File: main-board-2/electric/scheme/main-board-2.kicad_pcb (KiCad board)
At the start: 2 copper layers, 85 x 56 mm, 124 parts, among them K1 power-switch, K2 usb-power-switch, P1 batt, P10 rst, P11 screw-1, P13 screw-2, P14 gpio-big, P15 gpio-small, P16 moto-1, P17 moto-2, P3 trigger-btn, P4 CONN_3X2, P5 reg-short-to-gnd-1, P6 reg-short-to-gnd-2, P7 bootloader, P8 cross board conn, P9 rst, Q1 IRLML2244, Q10 IRLML2244, Q11 sot223, Q12 bc857, Q13 irlml2244, Q2 BC847, Q3 IRLML2244, Q4 IRLML2244, Q5 BC847, Q6 BC847, Q7 BC847, Q8 BC847, Q9 IRLML2244, U1 LM317AEMP, U2 LM317AT, U3 LM317AEMP, U4 LM317AT, U5 LM293, U6 L298, U7 MINI-USB-B, X1 8MHz

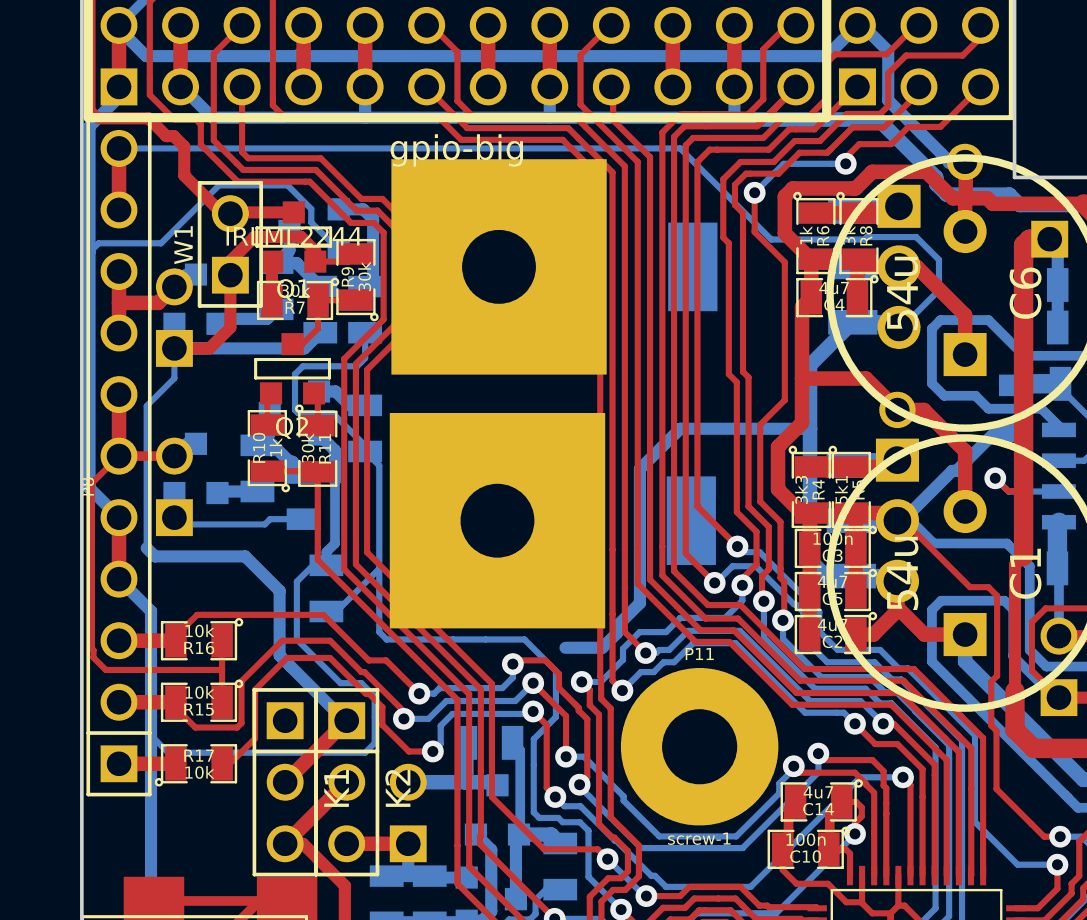
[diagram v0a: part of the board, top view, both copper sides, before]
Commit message: Changed packages to vertical ones.
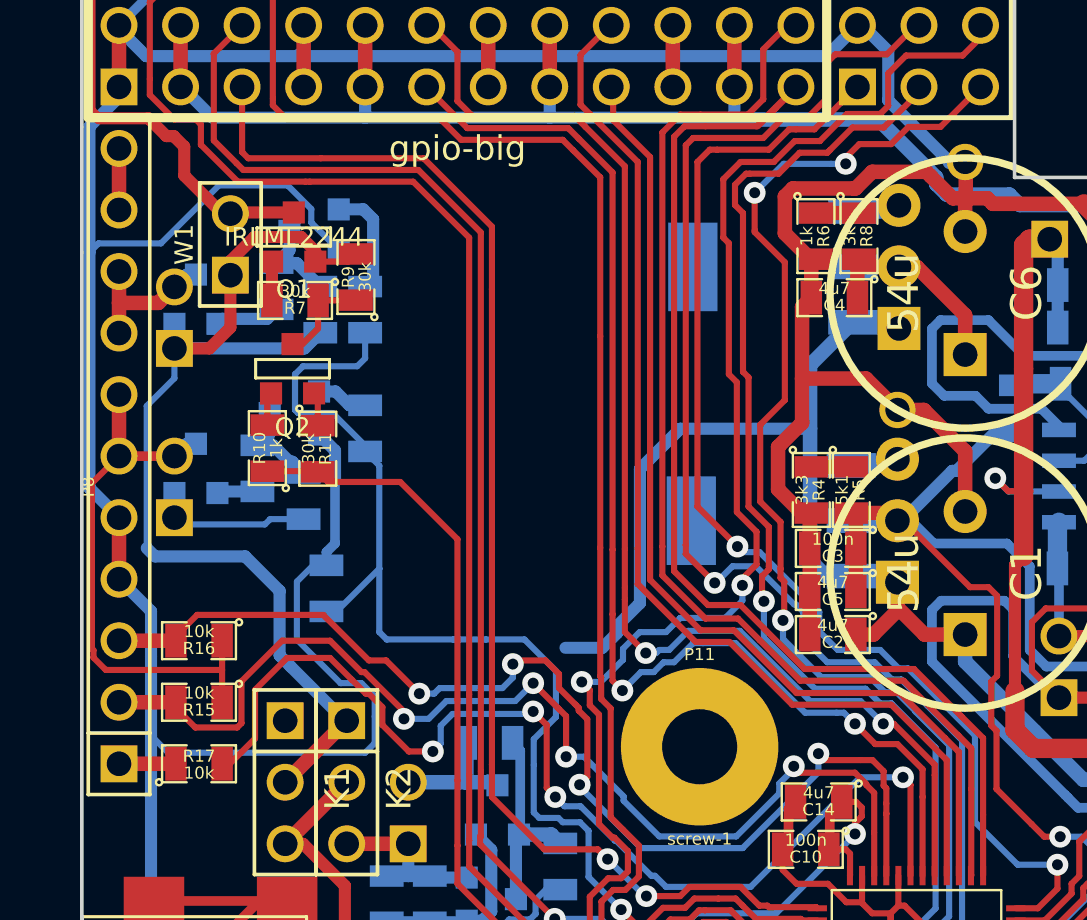
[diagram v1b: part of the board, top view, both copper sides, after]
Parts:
- U2, U4: footprint my_TO220 -> my_TO220_VERT
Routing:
- net /batt+: track 207.3 -> 164.3 mm
- net N-0000085: track 5.54 -> 3.47 mm
- net /rpi-pwr-en: track 49.0 -> 50.7 mm
- net N-0000086: track 6.06 -> 4.42 mm
- net /gpio-5: track 59.1 -> 59.8 mm
- net /gpio-1: track 52.9 -> 53.5 mm
- net /sda-rpi: track 77.5 -> 78.1 mm

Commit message: Routing...
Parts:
- moved R24 6.24 mm to (158.9, 153.3), turned to 0 degrees
- moved R22 6.10 mm to (161.2, 143.7)
- moved Q5 5.66 mm to (158.3, 143.8)
- moved Q6 5.08 mm to (157.1, 150.7)
- moved R11 4.98 mm to (157.9, 152.5)
- moved Q2 4.91 mm to (156.8, 149.2)
- moved R10 4.90 mm to (155.7, 152.5)
- moved R18 4.89 mm to (156.1, 142.2), turned to 180 degrees
- moved R19 4.89 mm to (154.9, 149.0), turned to 180 degrees
- moved Q3 4.66 mm to (152.8, 143.7), turned to 90 degrees
- moved R23 4.59 mm to (159.7, 150.7)
- moved R7 4.06 mm to (155.9, 146.5)
- moved R9 3.96 mm to (158.4, 145.4)
- moved Q1 3.95 mm to (155.9, 143.4)
- moved Q4 3.51 mm to (151.6, 150.5), turned to 90 degrees
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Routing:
- net /addon-pwr-en: track 49.9 -> 31.4 mm
- net /+5V: track 62.0 -> 52.6 mm
- net /rpi-pwr-en: track 50.7 -> 45.4 mm
- net /rx: track 61.5 -> 66.4 mm
- net /swd-io: track 66.6 -> 71.5 mm
- net GND: track 523.1 -> 518.6 mm
- net N-0000062: track 4.51 -> 0.00 mm
- net /gpio-9: track 48.7 -> 53.2 mm
- net /tx: track 61.5 -> 65.9 mm
- net /gpio-8: track 47.8 -> 51.3 mm
- net /swd-clk: track 63.5 -> 66.8 mm
- net /addon-5V: track 6.20 -> 9.44 mm
- net /gpio-4: track 47.4 -> 50.4 mm
- net N-000003: track 23.0 -> 25.8 mm
- net /gpio-7: track 45.1 -> 47.9 mm
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
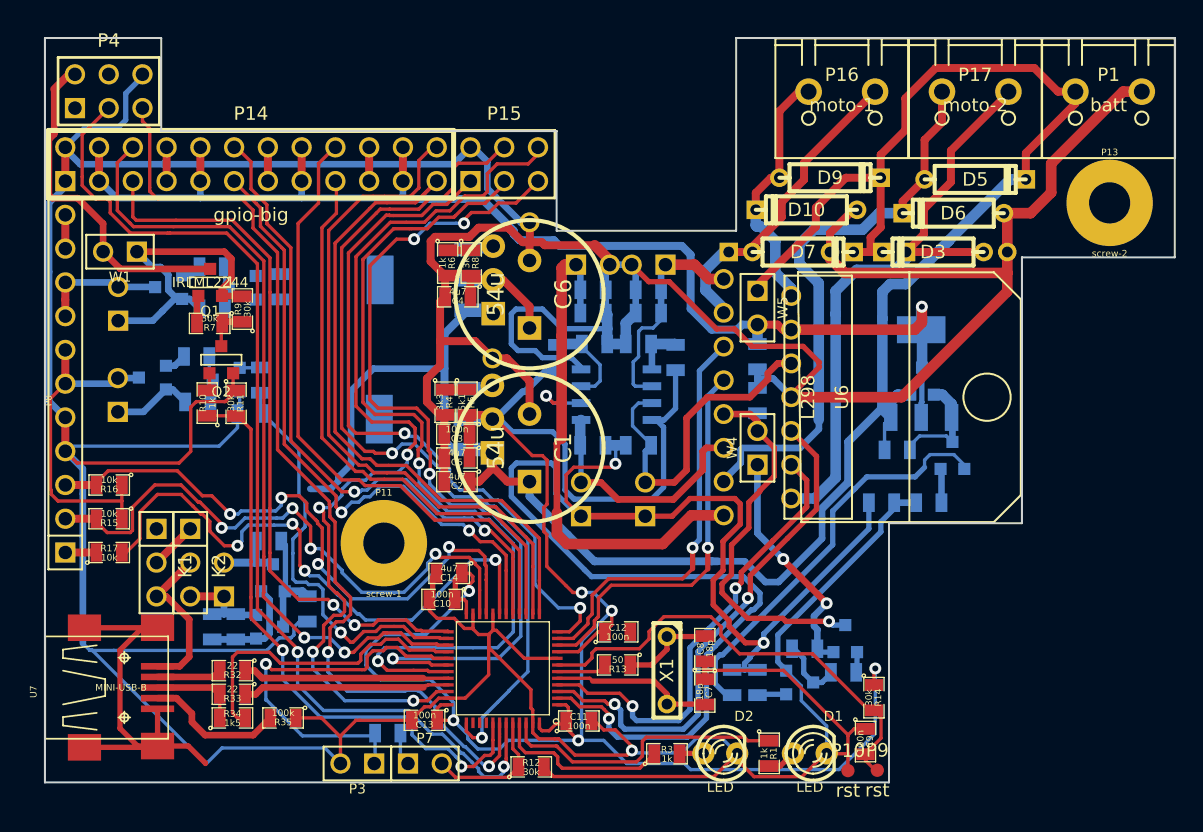
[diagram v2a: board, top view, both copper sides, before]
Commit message: Just one more circuit Vdd to addon socket last.
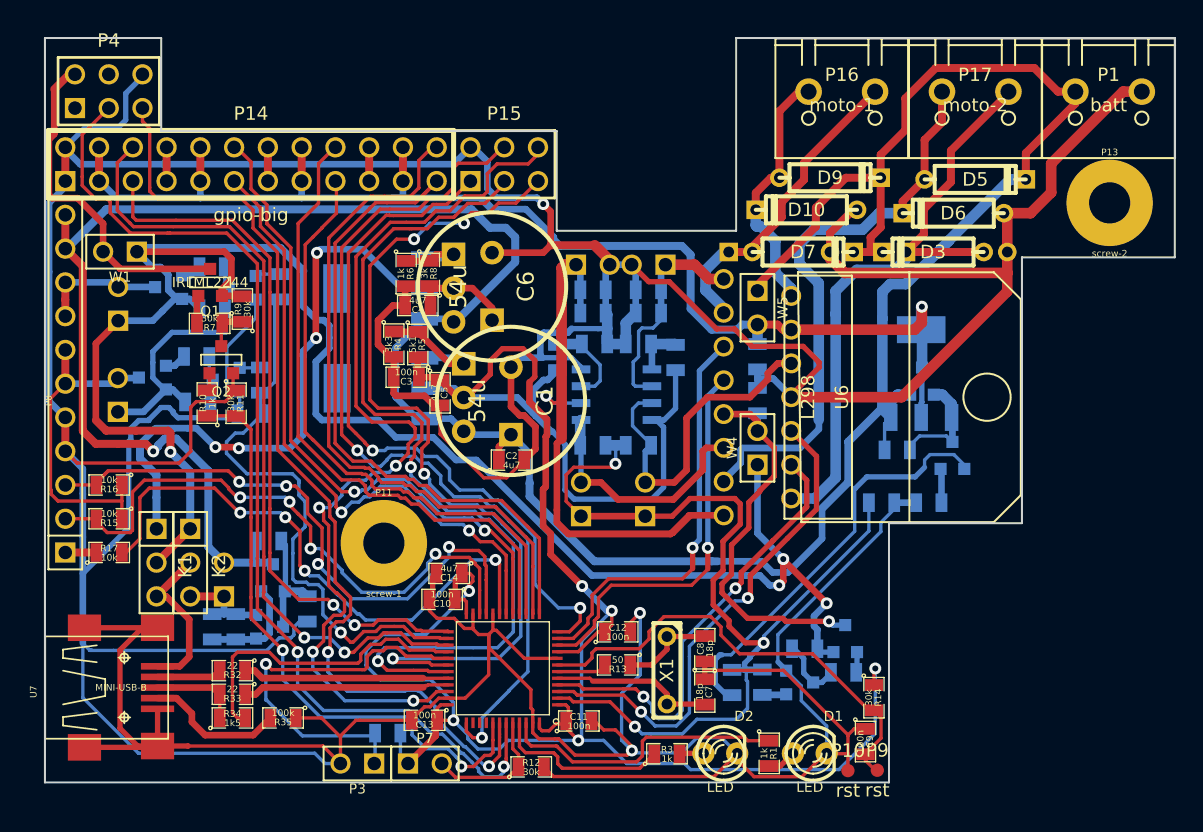
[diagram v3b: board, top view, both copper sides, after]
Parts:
- removed P5: reg-short-to-gnd-1, 1pin
- removed P6: reg-short-to-gnd-2, 1pin
- moved R4 5.83 mm to (169.7, 148.0)
- moved C3 5.74 mm to (170.7, 150.5)
- moved R5 5.71 mm to (171.6, 148.1)
- moved C5 5.06 mm to (173.2, 151.7), turned to 270 degrees
- moved C2 4.42 mm to (178.6, 156.8), turned to 0 degrees
- moved U1 3.93 mm to (168.8, 151.3)
- moved C1 3.80 mm to (178.6, 152.3)
- moved U3 3.33 mm to (168.8, 143.8)
- moved R8 3.25 mm to (172.4, 142.7)
- moved R6 3.23 mm to (170.7, 142.7)
- moved C4 3.08 mm to (171.6, 145.1)
- moved U4 3.05 mm to (174.2, 143.8), turned to 0 degrees
- moved C6 2.88 mm to (177.1, 143.7)
- moved U2 2.70 mm to (175.0, 152.0), turned to 0 degrees
- moved R27 0.37 mm to (197.5, 173.5)
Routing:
- net /+5V: track 52.6 -> 142.6 mm, vias 2 -> 4
- net /batt+: track 164.3 -> 229.9 mm, vias 0 -> 1
- net N-0000085: track 10.5 -> 54.4 mm, vias 0 -> 4
- net /moto-en: track 112.1 -> 74.8 mm
- net GND: track 518.6 -> 554.5 mm, vias 1 -> 3
- net VDD: track 164.9 -> 190.9 mm
- net /addon-pwr-en: track 31.4 -> 43.8 mm
- net /cur-sense-2: track 43.1 -> 55.4 mm
- net N-0000088: track 4.42 -> 9.37 mm
- net N-0000086: track 3.47 -> 6.07 mm
- net N-0000064: track 0.00 -> 1.86 mm
- net /gpio-3: track 43.6 -> 45.4 mm
- net N-0000048: track 28.1 -> 29.4 mm
- net /addon-trigger: track 44.8 -> 43.6 mm
- net /in-moto3: track 38.7 -> 37.8 mm
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
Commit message: Just connected all unconnected circuits.
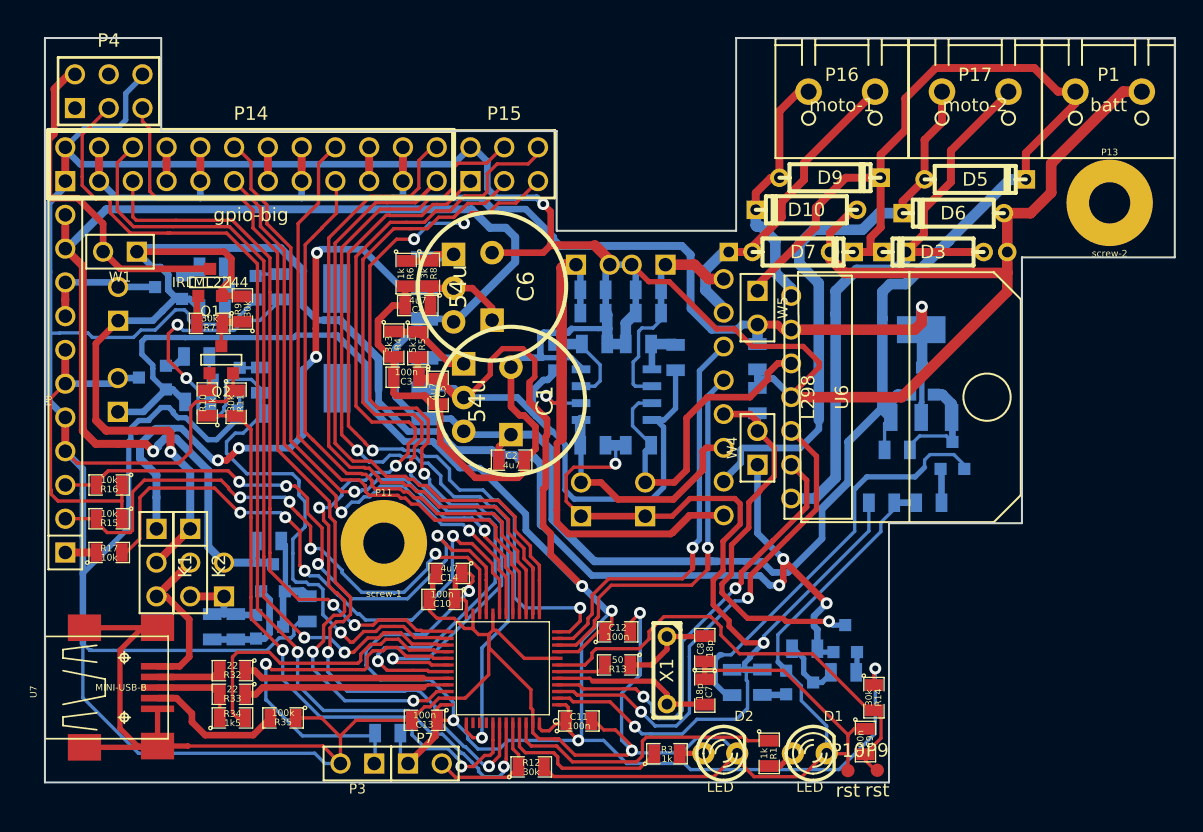
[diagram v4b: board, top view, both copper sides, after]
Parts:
- moved C5 0.18 mm to (173.1, 151.6)
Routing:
- net VDD: track 190.9 -> 229.5 mm
- net /addon-pwr-en: track 43.8 -> 60.6 mm, vias 1 -> 3
- net GND: track 554.5 -> 566.9 mm
- net /tx: track 66.3 -> 62.0 mm
- net /rx: track 66.8 -> 62.7 mm
- net /addon-trigger: track 43.6 -> 46.7 mm
- net /scl-int: track 47.0 -> 48.9 mm
- net /swd-clk: track 67.0 -> 65.4 mm
- net /gpio-9: track 53.4 -> 54.8 mm
- net /batt+: track 229.9 -> 230.9 mm
- net N-0000085: track 54.4 -> 55.1 mm
- net /+5V: track 142.6 -> 142.0 mm
- net /gpio-2: track 48.0 -> 47.5 mm

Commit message: Added comments.
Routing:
- added copper zone on B.Cu, net GND
- added copper zone on F.Cu, net GND
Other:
- board text added: "+ -"
- board text added: "1"
- board text added: "2"
- board text added: "3"
- board text added: "4"
- board text added: "5,1"
- board text added: "6,2"
- board text added: "7,3"
- board text added: "8,4"
- board text added: "V"
- board text added: "boot loader"
- board text added: "c,rx"
- board text added: "d,tx"
- board text added: "gnd"
- board text added: "gnd,9"
- board text added: "moto 1, 2, 3, 4"
- board text added: "pwr routing"
- board text added: "rst"
- board text added: "trigger"
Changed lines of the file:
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@@
     (area 127.606667 112.000001 242.964763 190.8)
     (thickness 1.6)
-    (drawings 57)
+    (drawings 84)
     (tracks 2008)
     (zones 0)
@@
     (pad_to_mask_clearance 0)
     (aux_axis_origin 143.5 181)
-    (visible_elements 7FFFFBFF)
+    (visible_elements 7FFFFFFF)
     (pcbplotparams
       (layerselection 3178497)
@@
     )
   )
+  (gr_text "pwr\nrouting" (at 155.5 158.5) (layer Cmts.User)
+    (effects (font (size 2 2) (thickness 0.3)) (justify left))
+  )
+  (gr_text 4 (at 158.25 165.75) (layer Cmts.User)
+    (effects (font (size 2 2) (thickness 0.3)))
+  )
+  (gr_text 3 (at 154.5 159.5) (layer Cmts.User)
+    (effects (font (size 2 2) (thickness 0.3)))
+  )
+  (gr_text 2 (at 151.5 159.5) (layer Cmts.User)
+    (effects (font (size 2 2) (thickness 0.3)))
+  )
+  (gr_text 1 (at 149.75 166.75) (layer Cmts.User)
+    (effects (font (size 2 2) (thickness 0.3)))
+  )
+  (gr_text gnd,9 (at 175.5 138.5 90) (layer Eco2.User)
+    (effects (font (size 1 1) (thickness 0.25)) (justify mirror))
+  )
+  (gr_text 8,4 (at 173 138.75 90) (layer Eco2.User)
+    (effects (font (size 1.5 1.5) (thickness 0.3)) (justify mirror))
+  )
+  (gr_text 7,3 (at 165.5 138.75 90) (layer Eco2.User)
+    (effects (font (size 1.5 1.5) (thickness 0.3)) (justify mirror))
+  )
+  (gr_text 6,2 (at 157.75 138.75 90) (layer Eco2.User)
+    (effects (font (size 1.5 1.5) (thickness 0.3)) (justify mirror))
+  )
+  (gr_text 5,1 (at 150.25 138.75 90) (layer Eco2.User)
+    (effects (font (size 1.5 1.5) (thickness 0.3)) (justify mirror))
+  )
+  (gr_text d,tx (at 180.5 138.75 90) (layer Eco2.User)
+    (effects (font (size 1.5 1.5) (thickness 0.3)) (justify mirror))
+  )
+  (gr_text c,rx (at 178 138.75 90) (layer Eco2.User)
+    (effects (font (size 1.5 1.5) (thickness 0.3)) (justify mirror))
+  )
+  (gr_text gnd (at 168 138.75 90) (layer Eco2.User)
+    (effects (font (size 1.5 1.5) (thickness 0.3)) (justify mirror))
+  )
+  (gr_text gnd (at 160.25 138.75 90) (layer Eco2.User)
+    (effects (font (size 1.5 1.5) (thickness 0.3)) (justify mirror))
+  )
+  (gr_text gnd (at 152.75 138.75 90) (layer Eco2.User)
+    (effects (font (size 1.5 1.5) (thickness 0.3)) (justify mirror))
+  )
+  (gr_text V (at 170.5 138.75 90) (layer Eco2.User)
+    (effects (font (size 2 2) (thickness 0.3)) (justify mirror))
+  )
+  (gr_text V (at 162.75 138.75 90) (layer Eco2.User)
+    (effects (font (size 2 2) (thickness 0.3)) (justify mirror))
+  )
+  (gr_text V (at 155.5 138.75 90) (layer Eco2.User)
+    (effects (font (size 2 2) (thickness 0.3)) (justify mirror))
+  )
+  (gr_text V (at 147.5 138.75 90) (layer Eco2.User)
+    (effects (font (size 2 2) (thickness 0.3)) (justify mirror))
+  )
+  (gr_text "boot\nloader" (at 170 172.5 90) (layer Eco2.User)
+    (effects (font (size 1.5 1.5) (thickness 0.3)) (justify mirror))
+  )
+  (gr_text trigger (at 166.75 173.5 90) (layer Eco2.User)
+    (effects (font (size 1.5 1.5) (thickness 0.3)) (justify mirror))
+  )
+  (gr_text "moto 1, 2, 3, 4" (at 208.25 132.5) (layer Eco2.User)
+    (effects (font (size 1.5 1.5) (thickness 0.3)) (justify mirror))
+  )
+  (gr_text "+ -" (at 223.5 133.5) (layer Eco2.User)
+    (effects (font (size 3 3) (thickness 0.3)))
+  )
+  (gr_text "boot\nloader" (at 169.75 172 90) (layer Cmts.User)
+    (effects (font (size 1.5 1.5) (thickness 0.3)))
+  )
+  (gr_text trigger (at 166.75 172.75 90) (layer Cmts.User)
+    (effects (font (size 1.5 1.5) (thickness 0.3)))
+  )
+  (gr_text rst (at 203.75 176.5 90) (layer Cmts.User)
+    (effects (font (size 1.5 1.5) (thickness 0.3)))
+  )
+  (gr_text "+ -" (at 223.5 133.5) (layer Cmts.User)
+    (effects (font (size 3 3) (thickness 0.3)))
+  )
   (gr_circle (center 160.655 153.67) (end 162.179 153.8478) (layer Dwgs.User) (width 0.2))
   (gr_circle (center 160.7312 143.2052) (end 162.2552 143.4338) (layer Dwgs.User) (width 0.2))
@@
   (segment (start 153.64206 172.26534) (end 154.3558 171.5516) (width 0.5) (layer F.Cu) (net 45))
   (segment (start 151.892 167.005) (end 154.432 164.465) (width 0.6) (layer F.Cu) (net 45))
-  (segment (start 179.56022 156.75356) (end 179.56022 157.62478) (width 0.5) (layer F.Cu) (net 46) (status 400000))
+  (segment (start 179.56022 156.75356) (end 179.56022 157.62478) (width 0.5) (layer F.Cu) (net 46))
   (segment (start 173.228 155.42768) (end 173.228 154.7876) (width 0.5) (layer F.Cu) (net 46))
   (segment (start 175.88484 158.08452) (end 173.228 155.42768) (width 0.5) (layer F.Cu) (net 46))
   (segment (start 179.10048 158.08452) (end 175.88484 158.08452) (width 0.5) (layer F.Cu) (net 46))
   (segment (start 179.56022 157.62478) (end 179.10048 158.08452) (width 0.5) (layer F.Cu) (net 46))
-  (segment (start 173.228 154.7876) (end 173.228 152.68702) (width 0.5) (layer F.Cu) (net 46) (status 800000))
-  (segment (start 173.228 152.68702) (end 173.08068 152.5397) (width 0.5) (layer F.Cu) (net 46) (status C00000))
+  (segment (start 173.228 154.7876) (end 173.228 152.68702) (width 0.5) (layer F.Cu) (net 46))
+  (segment (start 173.228 152.68702) (end 173.08068 152.5397) (width 0.5) (layer F.Cu) (net 46))
   (segment (start 173.08068 152.5397) (end 172.6819 152.5397) (width 0.6) (layer F.Cu) (net 46))
   (segment (start 172.6819 152.5397) (end 172.0596 151.9174) (width 0.6) (layer F.Cu) (net 46))
@@
   (segment (start 183.61914 171.16806) (end 185.1152 169.672) (width 0.254) (layer F.Cu) (net 83))
   (segment (start 185.1152 169.672) (end 185.6359 169.672) (width 0.254) (layer F.Cu) (net 83))
+  (zone (net 46) (net_name GND) (layer F.Cu) (hatch edge 0.508)
+    (connect_pads (clearance 0.508))
+    (min_thickness 0.254)
+    (fill (arc_segments 16) (thermal_gap 0.508) (thermal_bridge_width 0.508))
+    (polygon
+      (pts
+        (xy 228.5 141.5) (xy 217 141.5) (xy 217 161.5) (xy 207 161.5) (xy 207 181)
+        (xy 143.5 181) (xy 143.5 125) (xy 152.25 125) (xy 152.25 132) (xy 182 132)
+        (xy 182 139.5) (xy 195.5 139.5) (xy 195.5 125) (xy 228.5 125)
+      )
+    )
+  )
+  (zone (net 46) (net_name GND) (layer B.Cu) (hatch edge 0.508)
+    (connect_pads (clearance 0.508))
+    (min_thickness 0.254)
+    (fill (arc_segments 16) (thermal_gap 0.508) (thermal_bridge_width 0.508))
+    (polygon
+      (pts
+        (xy 228.5 141.5) (xy 217 141.5) (xy 217 161.5) (xy 207 161.5) (xy 207 181)
+        (xy 143.5 181) (xy 143.5 125) (xy 152.25 125) (xy 152.25 132) (xy 182 132)
+        (xy 182 139.5) (xy 195.5 139.5) (xy 195.5 125) (xy 228.5 125)
+      )
+    )
+  )
 )
